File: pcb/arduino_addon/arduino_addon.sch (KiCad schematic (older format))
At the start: 4 parts, among them P1 AnalogIn, P2 Power, P3 Digital1, P4 Digital2

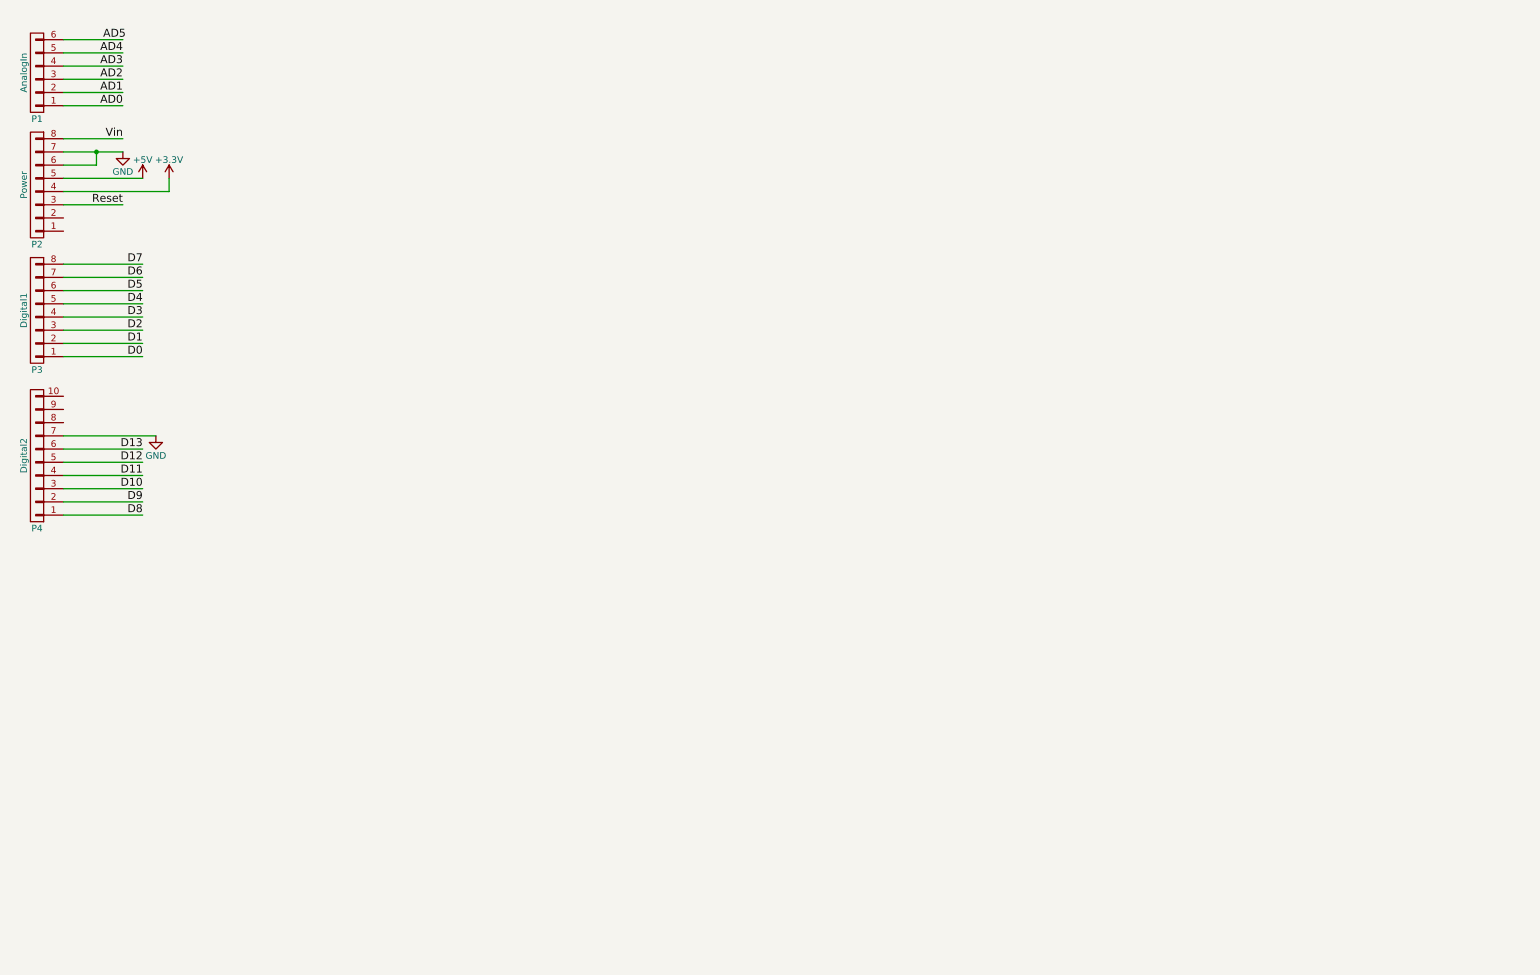
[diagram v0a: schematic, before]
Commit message: addon board schematic ready
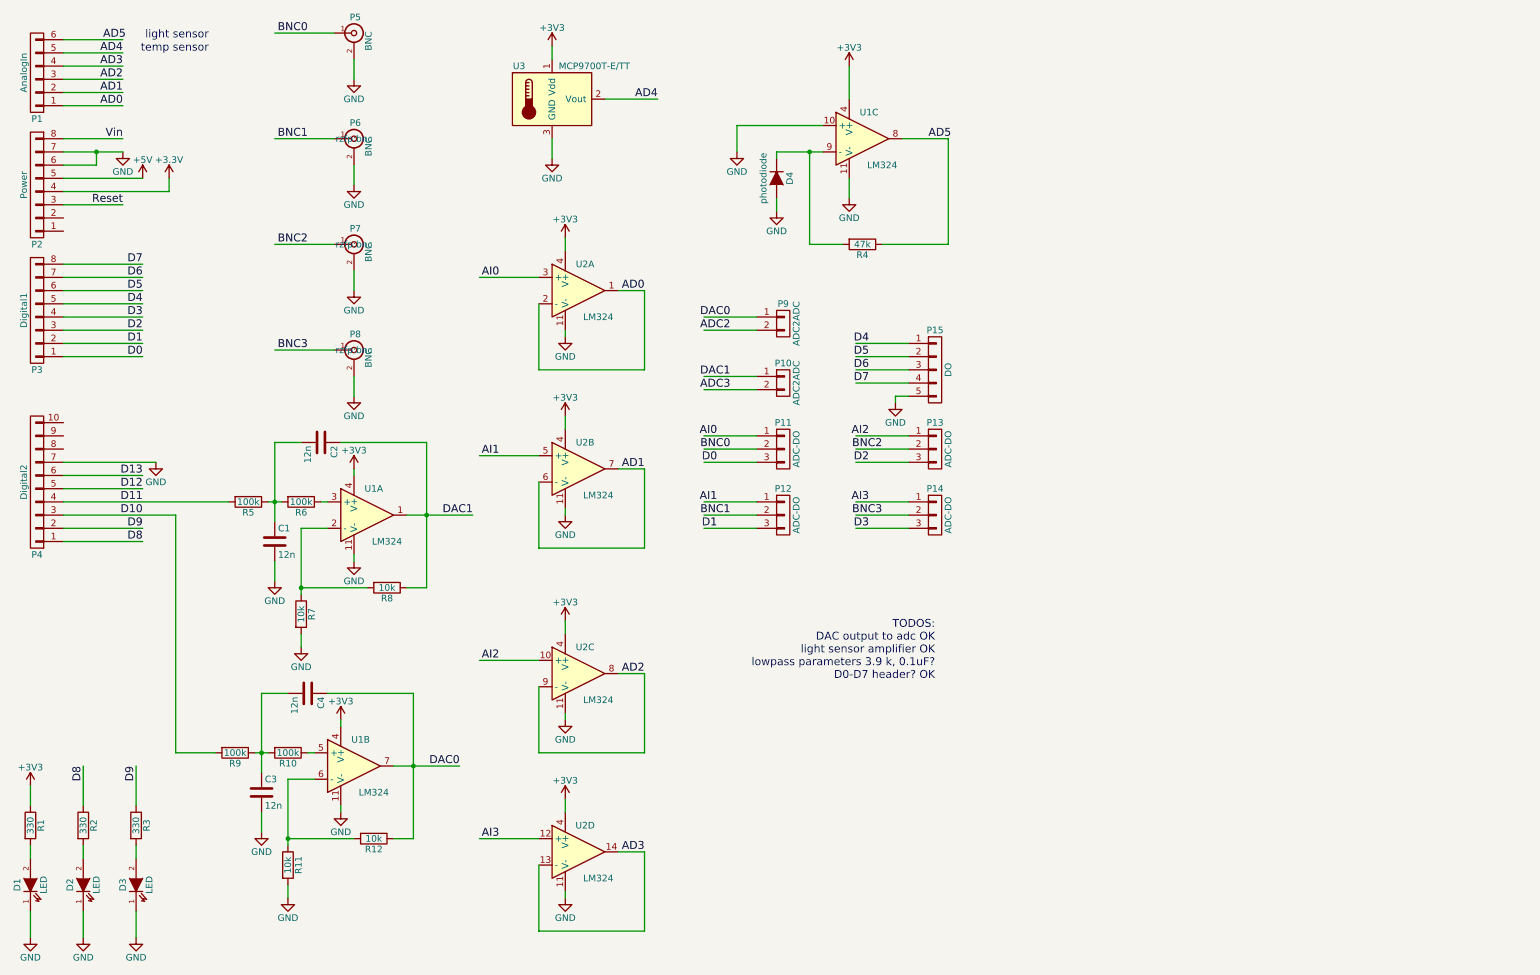
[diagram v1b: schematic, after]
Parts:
- added C1, C2, C3, C4: 12n, Capacitors_SMD:C_2220_HandSoldering, symbol C
- added D1, D2, D3: LED, LEDs:LED-3MM, symbol LED
- added D4: photodiode, Diodes_ThroughHole:Diode_DO-41_SOD81_Vertical_AnodeUp, symbol D
- added P10, P9: ADC2ADC, Pin_Headers:Pin_Header_Straight_1x02, symbol CONN_01X02
- added P11, P12, P13, P14: ADC-DO, Pin_Headers:Pin_Header_Straight_1x03, symbol CONN_01X03
- added P15: DO, Pin_Headers:Pin_Header_Straight_1x05, symbol CONN_01X05
- added P5, P6, P7, P8: BNC, rzfp:bnc, symbol BNC
- added R1, R2, R3: 330, Resistors_SMD:R_2512_HandSoldering, symbol R
- added R10, R5, R6, R9: 100k, Resistors_SMD:R_2512_HandSoldering, symbol R
- added R11, R12, R7, R8: 10k, Resistors_SMD:R_2512_HandSoldering, symbol R
- added R4: 47k, Resistors_SMD:R_2512_HandSoldering, symbol R
- added U1, U2: LM324, Housings_DIP:DIP-14_W7.62mm_LongPads, symbol LM324
- added U3: MCP9700T-E/TT, TO_SOT_Packages_THT:TO-92_Inline_Narrow_Oval, symbol MCP9700T-E/TT
- P2, P3: footprint (none) -> Pin_Headers:Pin_Header_Straight_1x08
- P4: footprint (none) -> Pin_Headers:Pin_Header_Straight_1x10
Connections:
- net labels added: +3V3, ADC2, ADC3, AI0, AI1, AI2, AI3, BNC0, BNC1, BNC2, BNC3, DAC0, DAC1
- wire segments 29 -> 143
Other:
- note added: "TODOS:\n DAC output to adc OK\n light sensor amplifier OK\n lowpass parameters 3.9 k, 0.1uF?\n D0-D7 header? OK"
- note added: "light sensor"
- note added: "temp sensor"
- moved on the sheet: P4

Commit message: pcb layout, no wiring
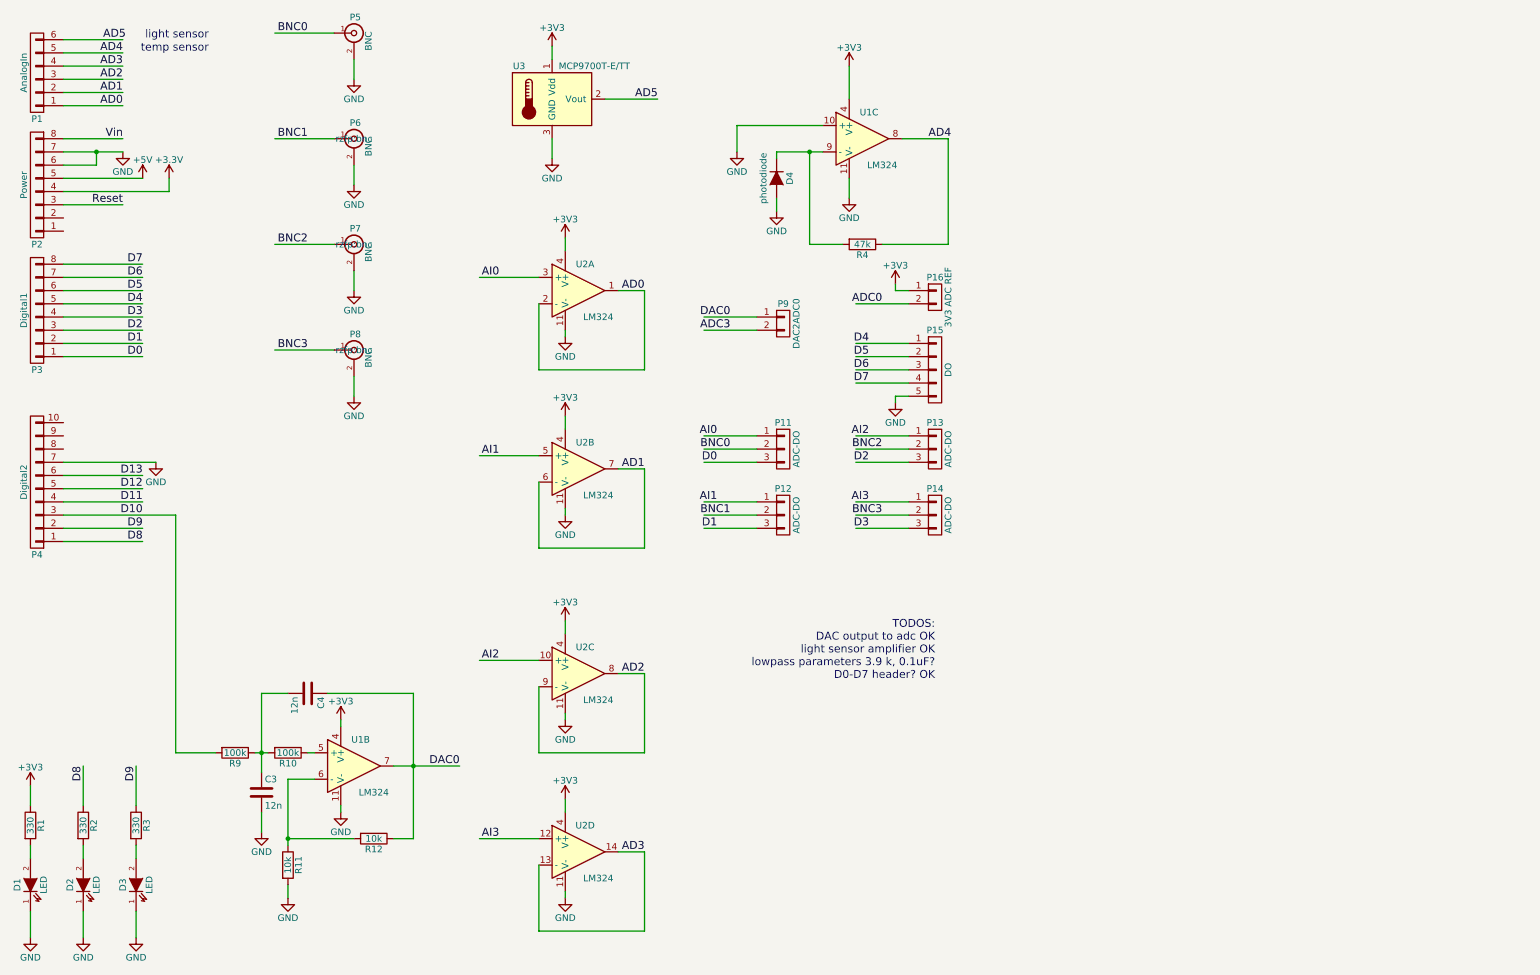
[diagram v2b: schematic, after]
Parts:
- removed C1, C2: 12n, Capacitors_SMD:C_2220_HandSoldering, symbol C
- removed P10: ADC2ADC, Pin_Headers:Pin_Header_Straight_1x02, symbol CONN_01X02
- removed R5, R6: 100k, Resistors_SMD:R_2512_HandSoldering, symbol R
- removed R7, R8: 10k, Resistors_SMD:R_2512_HandSoldering, symbol R
- removed unit 1 of U1
- added P16: 3V3 ADC REF, Pin_Headers:Pin_Header_Straight_1x02, symbol CONN_01X02
- P1: footprint (none) -> Pin_Headers:Pin_Header_Straight_1x06
- P9: value ADC2ADC -> DAC2ADC0
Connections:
- net labels added: ADC0
- net labels removed: ADC2, DAC1
- wire segments 143 -> 129
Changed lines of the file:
@@
 F 0 "P1" H 900 1350 50  0000 C CNN
 F 1 "AnalogIn" V 1000 1000 50  0000 C CNN
-F 2 "" H 900 1000 50  0000 C CNN
+F 2 "Pin_Headers:Pin_Header_Straight_1x06" H 900 1000 50  0001 C CNN
 F 3 "" H 900 1000 50  0000 C CNN
 	1    900  1000
@@
 $EndComp
 Text Label 5600 1200 2    60   ~ 0
-AD4
+AD5
 Text Notes 2200 750  2    60   ~ 0
 light sensor
-$Comp
-L LM324 U1
-U 1 1 58343607
-P 3400 4350
-F 0 "U1" H 3450 4550 50  0000 C CNN
-F 1 "LM324" H 3550 4150 50  0000 C CNN
-F 2 "Housings_DIP:DIP-14_W7.62mm_LongPads" H 3350 4450 50  0001 C CNN
-F 3 "" H 3450 4550 50  0000 C CNN
-F 4 "173-27-518" H 3400 4350 60  0001 C CNN "Part Number"
-	1    3400 4350
-	1    0    0    -1
-$EndComp
 $Comp
 L LM324 U1
@@
 	1    0    0    -1
 $EndComp
-$Comp
-L C C1
-U 1 1 58344AF1
-P 2700 4550
-F 0 "C1" H 2725 4650 50  0000 L CNN
-F 1 "12n" H 2725 4450 50  0000 L CNN
-F 2 "Capacitors_SMD:C_2220_HandSoldering" H 2738 4400 50  0001 C CNN
-F 3 "" H 2700 4550 50  0000 C CNN
-F 4 "300-10-943" H 2700 4550 60  0001 C CNN "Part Number"
-	1    2700 4550
-	1    0    0    -1
-$EndComp
-$Comp
-L GND #PWR012
-U 1 1 58344D42
-P 2700 4850
-F 0 "#PWR012" H 2700 4600 50  0001 C CNN
-F 1 "GND" H 2700 4700 50  0000 C CNN
-F 2 "" H 2700 4850 50  0000 C CNN
-F 3 "" H 2700 4850 50  0000 C CNN
-	1    2700 4850
-	1    0    0    -1
-$EndComp
-$Comp
-L GND #PWR013
-U 1 1 583451A9
-P 3300 4700
-F 0 "#PWR013" H 3300 4450 50  0001 C CNN
-F 1 "GND" H 3300 4550 50  0000 C CNN
-F 2 "" H 3300 4700 50  0000 C CNN
-F 3 "" H 3300 4700 50  0000 C CNN
-	1    3300 4700
-	1    0    0    -1
-$EndComp
-$Comp
-L +5V #PWR014
-U 1 1 5834528F
-P 3300 4000
-F 0 "#PWR014" H 3300 3850 50  0001 C CNN
-F 1 "+3V3" H 3300 4140 50  0000 C CNN
-F 2 "" H 3300 4000 50  0000 C CNN
-F 3 "" H 3300 4000 50  0000 C CNN
-	1    3300 4000
-	1    0    0    -1
-$EndComp
-Text Label 4200 4350 2    60   ~ 0
-DAC1
 $Comp
 L LED D2
@@
 	1100 4450 1700 4450
 Wire Wire Line
-	1100 4350 1950 4350
-Wire Wire Line
-	1100 4250 2350 4250
-Wire Wire Line
 	1100 3150 1700 3150
 Wire Wire Line
@@
 	5200 1200 5600 1200
 Wire Wire Line
-	2700 3800 2700 4400
-Wire Wire Line
-	2700 4700 2700 4850
-Wire Wire Line
-	3700 4350 4200 4350
-Wire Wire Line
-	2900 4450 3100 4450
-Wire Wire Line
-	3300 4000 3300 4050
-Connection ~ 3850 4350
-Wire Wire Line
 	1250 6250 1250 6550
 Wire Wire Line
@@
 Wire Wire Line
 	1650 7350 1650 7550
-Wire Wire Line
-	1950 4350 1950 6150
 Wire Wire Line
 	4700 2750 4700 3250
@@
 P 6550 2900
 F 0 "P9" H 6550 3050 50  0000 C CNN
-F 1 "ADC2ADC" V 6650 2900 50  0000 C CNN
+F 1 "DAC2ADC0" V 6650 2900 50  0000 C CNN
 F 2 "Pin_Headers:Pin_Header_Straight_1x02" H 6550 2900 50  0001 C CNN
 F 3 "" H 6550 2900 50  0000 C CNN
@@
 DAC0
 Text Label 6150 2950 2    60   ~ 0
-ADC2
-$Comp
-L CONN_01X02 P10
-U 1 1 5834D3A8
-P 6550 3350
-F 0 "P10" H 6550 3500 50  0000 C CNN
-F 1 "ADC2ADC" V 6650 3350 50  0000 C CNN
-F 2 "Pin_Headers:Pin_Header_Straight_1x02" H 6550 3350 50  0001 C CNN
-F 3 "" H 6550 3350 50  0000 C CNN
-	1    6550 3350
-	1    0    0    -1
-$EndComp
-Wire Wire Line
-	6350 3300 5950 3300
-Wire Wire Line
-	6350 3400 5950 3400
-Text Label 6150 3300 2    60   ~ 0
-DAC1
-Text Label 6150 3400 2    60   ~ 0
 ADC3
 $Comp
@@
 	7450 1500 7800 1500
 Text Label 7650 1500 0    60   ~ 0
-AD5
+AD4
 $Comp
 L R R4
@@
 $EndComp
 $Comp
-L R R8
-U 1 1 583870C0
-P 3550 4900
-F 0 "R8" V 3630 4900 50  0000 C CNN
-F 1 "10k" V 3550 4900 50  0000 C CNN
-F 2 "Resistors_SMD:R_2512_HandSoldering" V 3480 4900 50  0001 C CNN
-F 3 "" H 3550 4900 50  0000 C CNN
-F 4 "160-20-945" V 3550 4900 60  0001 C CNN "Part Number"
-	1    3550 4900
-	0    1    1    0
-$EndComp
-Wire Wire Line
-	3300 4650 3300 4700
-$Comp
-L R R7
-U 1 1 583873B3
-P 2900 5100
-F 0 "R7" V 2980 5100 50  0000 C CNN
-F 1 "10k" V 2900 5100 50  0000 C CNN
-F 2 "Resistors_SMD:R_2512_HandSoldering" V 2830 5100 50  0001 C CNN
-F 3 "" H 2900 5100 50  0000 C CNN
-F 4 "160-20-945" V 2900 5100 60  0001 C CNN "Part Number"
-	1    2900 5100
-	1    0    0    -1
-$EndComp
-Wire Wire Line
-	3850 3800 3850 4900
-Wire Wire Line
-	3850 4900 3700 4900
-Wire Wire Line
-	3400 4900 2900 4900
-Wire Wire Line
-	2900 4450 2900 4950
-Connection ~ 2900 4900
-Wire Wire Line
-	2900 5250 2900 5350
-$Comp
-L GND #PWR030
-U 1 1 58387860
-P 2900 5350
-F 0 "#PWR030" H 2900 5100 50  0001 C CNN
-F 1 "GND" H 2900 5200 50  0000 C CNN
-F 2 "" H 2900 5350 50  0000 C CNN
-F 3 "" H 2900 5350 50  0000 C CNN
-	1    2900 5350
-	1    0    0    -1
-$EndComp
-$Comp
-L R R6
-U 1 1 58388667
-P 2900 4250
-F 0 "R6" V 2980 4250 50  0000 C CNN
-F 1 "100k" V 2900 4250 50  0000 C CNN
-F 2 "Resistors_SMD:R_2512_HandSoldering" V 2830 4250 50  0001 C CNN
-F 3 "" H 2900 4250 50  0000 C CNN
-F 4 "160-21-067" V 2900 4250 60  0001 C CNN "Part Number"
-	1    2900 4250
-	0    1    1    0
-$EndComp
-$Comp
-L R R5
-U 1 1 583887C6
-P 2500 4250
-F 0 "R5" V 2580 4250 50  0000 C CNN
-F 1 "100k" V 2500 4250 50  0000 C CNN
-F 2 "Resistors_SMD:R_2512_HandSoldering" V 2430 4250 50  0001 C CNN
-F 3 "" H 2500 4250 50  0000 C CNN
-F 4 "160-21-067" V 2500 4250 60  0001 C CNN "Part Number"
-	1    2500 4250
-	0    1    1    0
-$EndComp
-Wire Wire Line
-	2650 4250 2750 4250
-Wire Wire Line
-	3050 4250 3100 4250
-Connection ~ 2700 4250
-$Comp
-L C C2
-U 1 1 58388CEB
-P 3050 3800
-F 0 "C2" H 3075 3900 50  0000 L CNN
-F 1 "12n" H 3075 3700 50  0000 L CNN
-F 2 "Capacitors_SMD:C_2220_HandSoldering" H 3088 3650 50  0001 C CNN
-F 3 "" H 3050 3800 50  0000 C CNN
-F 4 "300-10-943" H 3050 3800 60  0001 C CNN "Part Number"
-	1    3050 3800
-	0    1    1    0
-$EndComp
-Wire Wire Line
-	3200 3800 3850 3800
-Wire Wire Line
-	2900 3800 2700 3800
-$Comp
 L LM324 U1
 U 2 1 5838D927
@@
 	1    0    0    -1
 $EndComp
+$Comp
+L CONN_01X02 P16
+U 1 1 58394226
+P 7700 2700
+F 0 "P16" H 7700 2850 50  0000 C CNN
+F 1 "3V3 ADC REF" V 7800 2700 50  0000 C CNN
+F 2 "Pin_Headers:Pin_Header_Straight_1x02" H 7700 2700 50  0001 C CNN
+F 3 "" H 7700 2700 50  0000 C CNN
+	1    7700 2700
+	1    0    0    -1
+$EndComp
+Wire Wire Line
+	7500 2750 7100 2750
+Text Label 7300 2750 2    60   ~ 0
+ADC0
+Wire Wire Line
+	7500 2650 7400 2650
+Wire Wire Line
+	7400 2650 7400 2600
+$Comp
+L +3V3 #PWR036
+U 1 1 583944B9
+P 7400 2600
+F 0 "#PWR036" H 7400 2450 50  0001 C CNN
+F 1 "+3V3" H 7400 2740 50  0000 C CNN
+F 2 "" H 7400 2600 50  0000 C CNN
+F 3 "" H 7400 2600 50  0000 C CNN
+	1    7400 2600
+	1    0    0    -1
+$EndComp
+Wire Wire Line
+	1100 4350 1950 4350
+Wire Wire Line
+	1950 4350 1950 6150
+Wire Wire Line
+	1100 4250 1700 4250
 $EndSCHEMATC
